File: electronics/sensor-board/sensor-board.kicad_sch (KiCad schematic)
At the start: 0 parts

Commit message: Added title to sensor board
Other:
- note added: "Sensor Board"
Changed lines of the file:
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@@
 (kicad_sch (version 20210621) (generator eeschema)
   (paper "A4")
-  (symbol_instances)
+  (text "Sensor Board" (at 186.436 191.008 0)
+    (effects (font (size 2 2)) (justify left bottom))
+  )
+  (sheet_instances
+    (path "/" (page "1"))
+  )
 )

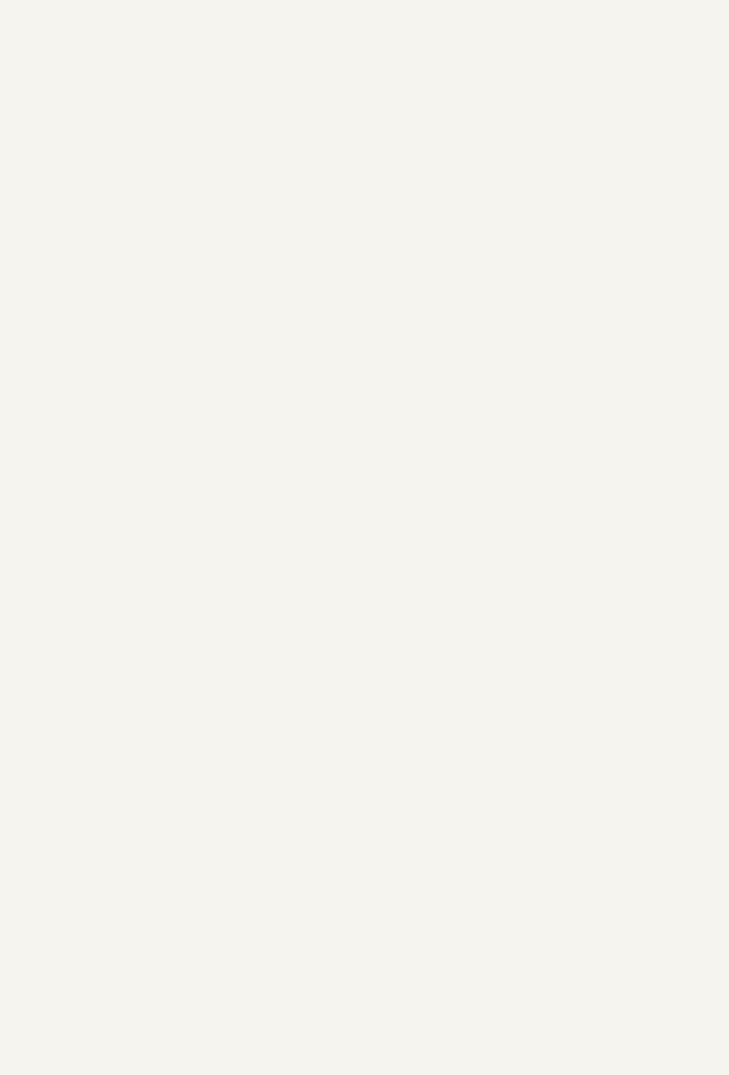
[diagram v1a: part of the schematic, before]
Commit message: Added libraries to sensor board pcb schematic
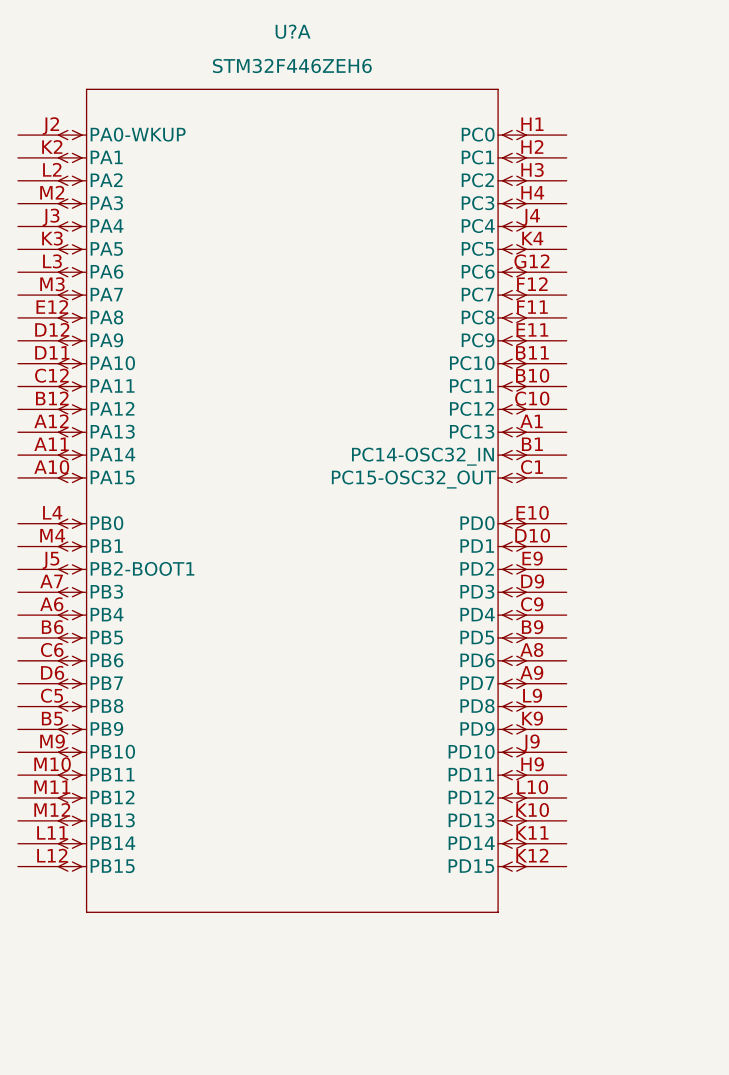
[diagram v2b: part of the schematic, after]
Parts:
- added U?: STM32F446ZEH6, UFBGA144-7x7x0P6, symbol STM32F446ZEH6:STM32F446ZEH6
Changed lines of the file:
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@@
     (effects (font (size 2 2)) (justify left bottom))
+  )
+  (symbol (lib_id "STM32F446ZEH6:STM32F446ZEH6") (at 124.46 59.69 0) (unit 1)
+    (in_bom yes) (on_board yes) (fields_autoplaced)
+    (property "Reference" "U?" (id 0) (at 154.94 48.26 0)
+      (effects (font (size 1.524 1.524)))
+    )
+    (property "Value" "STM32F446ZEH6" (id 1) (at 154.94 52.07 0)
+      (effects (font (size 1.524 1.524)))
+    )
+    (property "Footprint" "UFBGA144-7x7x0P6" (id 2) (at 154.94 53.594 0)
+      (effects (font (size 1.524 1.524)) hide)
+    )
+    (property "Datasheet" "" (id 3) (at 124.46 59.69 0)
+      (effects (font (size 1.524 1.524)))
+    )
+    (pin "A1")
+    (pin "A10")
+    (pin "A11")
+    (pin "A12")
+    (pin "A6")
+    (pin "A7")
+    (pin "A8")
+    (pin "A9")
+    (pin "B1")
+    (pin "B10")
+    (pin "B11")
+    (pin "B12")
+    (pin "B5")
+    (pin "B6")
+    (pin "B9")
+    (pin "C1")
+    (pin "C10")
+    (pin "C12")
+    (pin "C5")
+    (pin "C6")
+    (pin "C9")
+    (pin "D10")
+    (pin "D11")
+    (pin "D12")
+    (pin "D6")
+    (pin "D9")
+    (pin "E10")
+    (pin "E11")
+    (pin "E12")
+    (pin "E9")
+    (pin "F11")
+    (pin "F12")
+    (pin "G12")
+    (pin "H1")
+    (pin "H2")
+    (pin "H3")
+    (pin "H4")
+    (pin "H9")
+    (pin "J2")
+    (pin "J3")
+    (pin "J4")
+    (pin "J5")
+    (pin "J9")
+    (pin "K10")
+    (pin "K11")
+    (pin "K12")
+    (pin "K2")
+    (pin "K3")
+    (pin "K4")
+    (pin "K9")
+    (pin "L10")
+    (pin "L11")
+    (pin "L12")
+    (pin "L2")
+    (pin "L3")
+    (pin "L4")
+    (pin "L9")
+    (pin "M10")
+    (pin "M11")
+    (pin "M12")
+    (pin "M2")
+    (pin "M3")
+    (pin "M4")
+    (pin "M9")
   )
   (sheet_instances
     (path "/" (page "1"))
   )
+  (symbol_instances
+    (path "/5e75d057-7926-459c-a260-4ddabf512390"
+      (reference "U?") (unit 1) (value "STM32F446ZEH6") (footprint "UFBGA144-7x7x0P6")
+    )
+  )
 )

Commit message: Moved stm32 datasheet in appropriate folder
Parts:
- added U?: ADS114S08BIPBSR, PBS0032A_N, symbol ADS114S08BIPBSR:ADS114S08BIPBSR
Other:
- moved on the sheet: U?A
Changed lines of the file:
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@@
     (effects (font (size 2 2)) (justify left bottom))
   )
-  (symbol (lib_id "STM32F446ZEH6:STM32F446ZEH6") (at 124.46 59.69 0) (unit 1)
+  (symbol (lib_id "ADS114S08BIPBSR:ADS114S08BIPBSR") (at 78.74 74.93 0) (unit 1)
     (in_bom yes) (on_board yes) (fields_autoplaced)
-    (property "Reference" "U?" (id 0) (at 154.94 48.26 0)
+    (property "Reference" "U?" (id 0) (at 78.74 27.94 0)
       (effects (font (size 1.524 1.524)))
     )
-    (property "Value" "STM32F446ZEH6" (id 1) (at 154.94 52.07 0)
+    (property "Value" "ADS114S08BIPBSR" (id 1) (at 78.74 31.75 0)
       (effects (font (size 1.524 1.524)))
     )
-    (property "Footprint" "UFBGA144-7x7x0P6" (id 2) (at 154.94 53.594 0)
+    (property "Footprint" "PBS0032A_N" (id 2) (at 78.74 76.454 0)
       (effects (font (size 1.524 1.524)) hide)
     )
-    (property "Datasheet" "" (id 3) (at 124.46 59.69 0)
+    (property "Datasheet" "" (id 3) (at 78.74 74.93 0)
+      (effects (font (size 1.524 1.524)))
+    )
+    (pin "1")
+    (pin "10")
+    (pin "11")
+    (pin "12")
+    (pin "13")
+    (pin "14")
+    (pin "15")
+    (pin "16")
+    (pin "17")
+    (pin "18")
+    (pin "19")
+    (pin "2")
+    (pin "20")
+    (pin "21")
+    (pin "22")
+    (pin "23")
+    (pin "24")
+    (pin "25")
+    (pin "26")
+    (pin "27")
+    (pin "28")
+    (pin "29")
+    (pin "3")
+    (pin "30")
+    (pin "31")
+    (pin "32")
+    (pin "4")
+    (pin "5")
+    (pin "6")
+    (pin "7")
+    (pin "8")
+    (pin "9")
+  )
+  (symbol (lib_id "STM32F446ZEH6:STM32F446ZEH6") (at 161.29 35.56 0) (unit 1)
+    (in_bom yes) (on_board yes) (fields_autoplaced)
+    (property "Reference" "U?" (id 0) (at 191.77 24.13 0)
+      (effects (font (size 1.524 1.524)))
+    )
+    (property "Value" "STM32F446ZEH6" (id 1) (at 191.77 27.94 0)
+      (effects (font (size 1.524 1.524)))
+    )
+    (property "Footprint" "UFBGA144-7x7x0P6" (id 2) (at 191.77 29.464 0)
+      (effects (font (size 1.524 1.524)) hide)
+    )
+    (property "Datasheet" "" (id 3) (at 161.29 35.56 0)
       (effects (font (size 1.524 1.524)))
     )
@@
   )
   (symbol_instances
+    (path "/5d250a10-0c2b-4558-83a8-c06ab8b0eb20"
+      (reference "U?") (unit 1) (value "ADS114S08BIPBSR") (footprint "PBS0032A_N")
+    )
     (path "/5e75d057-7926-459c-a260-4ddabf512390"
       (reference "U?") (unit 1) (value "STM32F446ZEH6") (footprint "UFBGA144-7x7x0P6")

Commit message: Schematic edit
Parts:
- removed U?: ADS114S08BIPBSR, PBS0032A_N, symbol ADS114S08BIPBSR:ADS114S08BIPBSR
- removed U?: STM32F446ZEH6, UFBGA144-7x7x0P6, symbol STM32F446ZEH6:STM32F446ZEH6
- added U1: STM32F446ZEH6, STM32F446ZEH6:STM32F446ZEH6, symbol STM32F446ZEH6:STM32F446ZEH6
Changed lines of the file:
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@@
     (effects (font (size 2 2)) (justify left bottom))
   )
-  (symbol (lib_id "ADS114S08BIPBSR:ADS114S08BIPBSR") (at 78.74 74.93 0) (unit 1)
+  (symbol (lib_id "STM32F446ZEH6:STM32F446ZEH6") (at 73.66 139.7 0) (unit 3)
     (in_bom yes) (on_board yes) (fields_autoplaced)
-    (property "Reference" "U?" (id 0) (at 78.74 27.94 0)
-      (effects (font (size 1.524 1.524)))
-    )
-    (property "Value" "ADS114S08BIPBSR" (id 1) (at 78.74 31.75 0)
-      (effects (font (size 1.524 1.524)))
-    )
-    (property "Footprint" "PBS0032A_N" (id 2) (at 78.74 76.454 0)
+    (property "Reference" "U1" (id 0) (at 96.52 128.27 0)
+      (effects (font (size 1.524 1.524)))
+    )
+    (property "Value" "STM32F446ZEH6" (id 1) (at 96.52 132.08 0)
+      (effects (font (size 1.524 1.524)))
+    )
+    (property "Footprint" "STM32F446ZEH6:STM32F446ZEH6" (id 2) (at 104.14 133.604 0)
       (effects (font (size 1.524 1.524)) hide)
     )
-    (property "Datasheet" "" (id 3) (at 78.74 74.93 0)
-      (effects (font (size 1.524 1.524)))
-    )
-    (pin "1")
-    (pin "10")
-    (pin "11")
-    (pin "12")
-    (pin "13")
-    (pin "14")
-    (pin "15")
-    (pin "16")
-    (pin "17")
-    (pin "18")
-    (pin "19")
-    (pin "2")
-    (pin "20")
-    (pin "21")
-    (pin "22")
-    (pin "23")
-    (pin "24")
-    (pin "25")
-    (pin "26")
-    (pin "27")
-    (pin "28")
-    (pin "29")
-    (pin "3")
-    (pin "30")
-    (pin "31")
-    (pin "32")
-    (pin "4")
-    (pin "5")
-    (pin "6")
-    (pin "7")
-    (pin "8")
-    (pin "9")
-  )
-  (symbol (lib_id "STM32F446ZEH6:STM32F446ZEH6") (at 161.29 35.56 0) (unit 1)
+    (property "Datasheet" "" (id 3) (at 73.66 139.7 0)
+      (effects (font (size 1.524 1.524)))
+    )
+    (pin "C11")
+    (pin "C2")
+    (pin "D2")
+    (pin "D3")
+    (pin "E6")
+    (pin "E7")
+    (pin "F10")
+    (pin "F4")
+    (pin "F5")
+    (pin "F6")
+    (pin "F7")
+    (pin "F8")
+    (pin "F9")
+    (pin "G10")
+    (pin "G4")
+    (pin "G5")
+    (pin "G6")
+    (pin "G7")
+    (pin "G8")
+    (pin "G9")
+    (pin "H6")
+    (pin "H7")
+    (pin "J1")
+    (pin "K1")
+    (pin "L1")
+    (pin "M1")
+  )
+  (symbol (lib_id "STM32F446ZEH6:STM32F446ZEH6") (at 125.73 36.83 0) (unit 1)
     (in_bom yes) (on_board yes) (fields_autoplaced)
-    (property "Reference" "U?" (id 0) (at 191.77 24.13 0)
-      (effects (font (size 1.524 1.524)))
-    )
-    (property "Value" "STM32F446ZEH6" (id 1) (at 191.77 27.94 0)
-      (effects (font (size 1.524 1.524)))
-    )
-    (property "Footprint" "UFBGA144-7x7x0P6" (id 2) (at 191.77 29.464 0)
+    (property "Reference" "U1" (id 0) (at 156.21 25.4 0)
+      (effects (font (size 1.524 1.524)))
+    )
+    (property "Value" "STM32F446ZEH6" (id 1) (at 156.21 29.21 0)
+      (effects (font (size 1.524 1.524)))
+    )
+    (property "Footprint" "STM32F446ZEH6:STM32F446ZEH6" (id 2) (at 156.21 30.734 0)
       (effects (font (size 1.524 1.524)) hide)
     )
-    (property "Datasheet" "" (id 3) (at 161.29 35.56 0)
+    (property "Datasheet" "" (id 3) (at 125.73 36.83 0)
       (effects (font (size 1.524 1.524)))
     )
@@
     (pin "M9")
   )
+  (symbol (lib_id "STM32F446ZEH6:STM32F446ZEH6") (at 191.77 35.56 0) (unit 2)
+    (in_bom yes) (on_board yes) (fields_autoplaced)
+    (property "Reference" "U1" (id 0) (at 224.79 24.13 0)
+      (effects (font (size 1.524 1.524)))
+    )
+    (property "Value" "STM32F446ZEH6" (id 1) (at 224.79 27.94 0)
+      (effects (font (size 1.524 1.524)))
+    )
+    (property "Footprint" "STM32F446ZEH6:STM32F446ZEH6" (id 2) (at 222.25 29.464 0)
+      (effects (font (size 1.524 1.524)) hide)
+    )
+    (property "Datasheet" "" (id 3) (at 191.77 35.56 0)
+      (effects (font (size 1.524 1.524)))
+    )
+    (pin "A2")
+    (pin "A3")
+    (pin "A4")
+    (pin "A5")
+    (pin "B2")
+    (pin "B3")
+    (pin "B4")
+    (pin "B7")
+    (pin "B8")
+    (pin "C3")
+    (pin "C4")
+    (pin "C7")
+    (pin "C8")
+    (pin "D1")
+    (pin "D4")
+    (pin "D5")
+    (pin "D7")
+    (pin "D8")
+    (pin "E1")
+    (pin "E2")
+    (pin "E3")
+    (pin "E4")
+    (pin "E5")
+    (pin "E8")
+    (pin "F1")
+    (pin "F2")
+    (pin "F3")
+    (pin "G1")
+    (pin "G11")
+    (pin "G2")
+    (pin "G3")
+    (pin "H10")
+    (pin "H11")
+    (pin "H12")
+    (pin "H5")
+    (pin "H8")
+    (pin "J10")
+    (pin "J11")
+    (pin "J12")
+    (pin "J6")
+    (pin "J7")
+    (pin "J8")
+    (pin "K5")
+    (pin "K6")
+    (pin "K7")
+    (pin "K8")
+    (pin "L5")
+    (pin "L6")
+    (pin "L7")
+    (pin "L8")
+    (pin "M5")
+    (pin "M6")
+    (pin "M7")
+    (pin "M8")
+  )
   (sheet_instances
     (path "/" (page "1"))
   )
   (symbol_instances
-    (path "/5d250a10-0c2b-4558-83a8-c06ab8b0eb20"
-      (reference "U?") (unit 1) (value "ADS114S08BIPBSR") (footprint "PBS0032A_N")
-    )
-    (path "/5e75d057-7926-459c-a260-4ddabf512390"
-      (reference "U?") (unit 1) (value "STM32F446ZEH6") (footprint "UFBGA144-7x7x0P6")
-    )
-  )
+    (path "/dce51239-dcb2-4c77-beeb-0a51b252b6e3"
+      (reference "U1") (unit 1) (value "STM32F446ZEH6") (footprint "STM32F446ZEH6:STM32F446ZEH6")
+    )
+    (path "/119a3393-c07e-4ab6-a225-a008f184cdbd"
+      (reference "U1") (unit 2) (value "STM32F446ZEH6") (footprint "STM32F446ZEH6:STM32F446ZEH6")
+    )
+    (path "/ed637436-c1a3-4798-a3fe-f67431851823"
+      (reference "U1") (unit 3) (value "STM32F446ZEH6") (footprint "STM32F446ZEH6:STM32F446ZEH6")
+    )
+  )
